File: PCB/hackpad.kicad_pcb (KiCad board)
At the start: 2 copper layers, 123.8 x 50 mm, 11 parts, among them SW1 SW_Push, SW2 SW_Push, SW3 SW_Push, SW4 SW_Push, SW5 SW_Push, SW7 SW_Push, U1 XIAO-RP2040-DIP

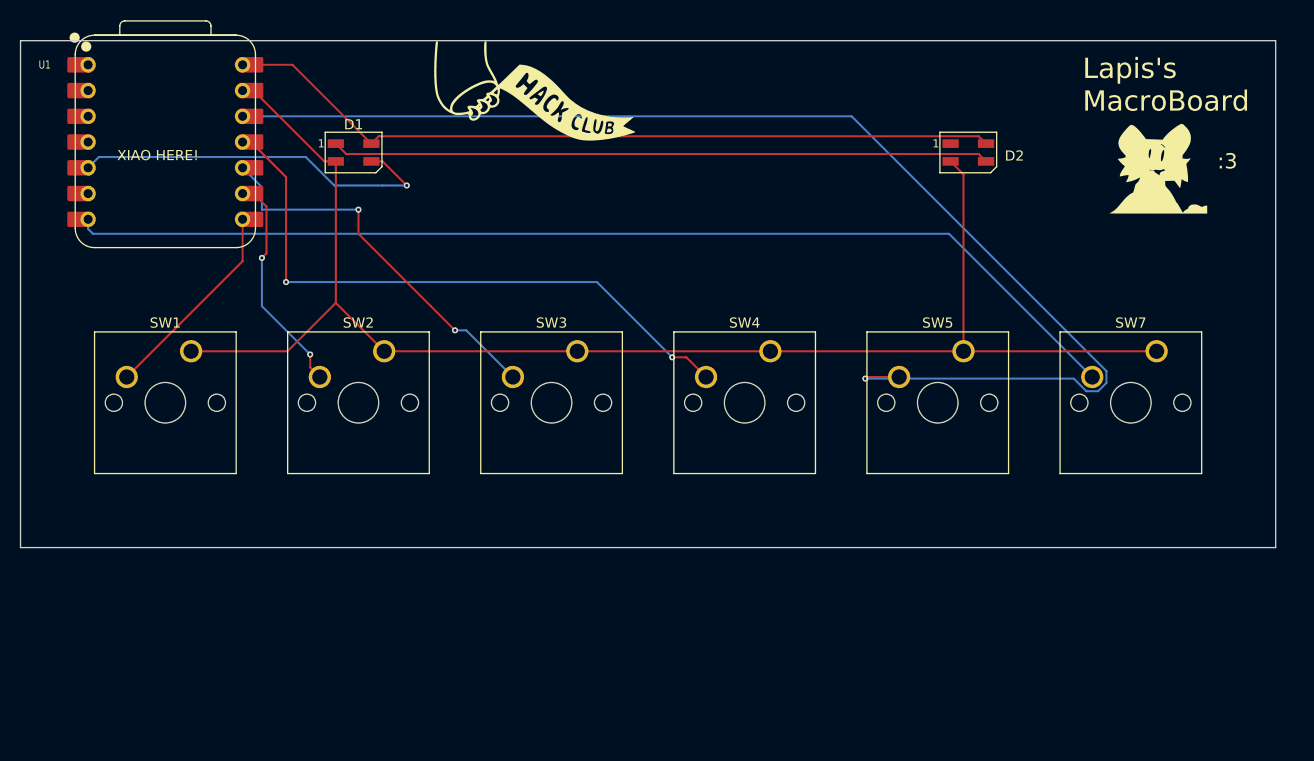
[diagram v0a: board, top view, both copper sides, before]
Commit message: push updated pcb and cad
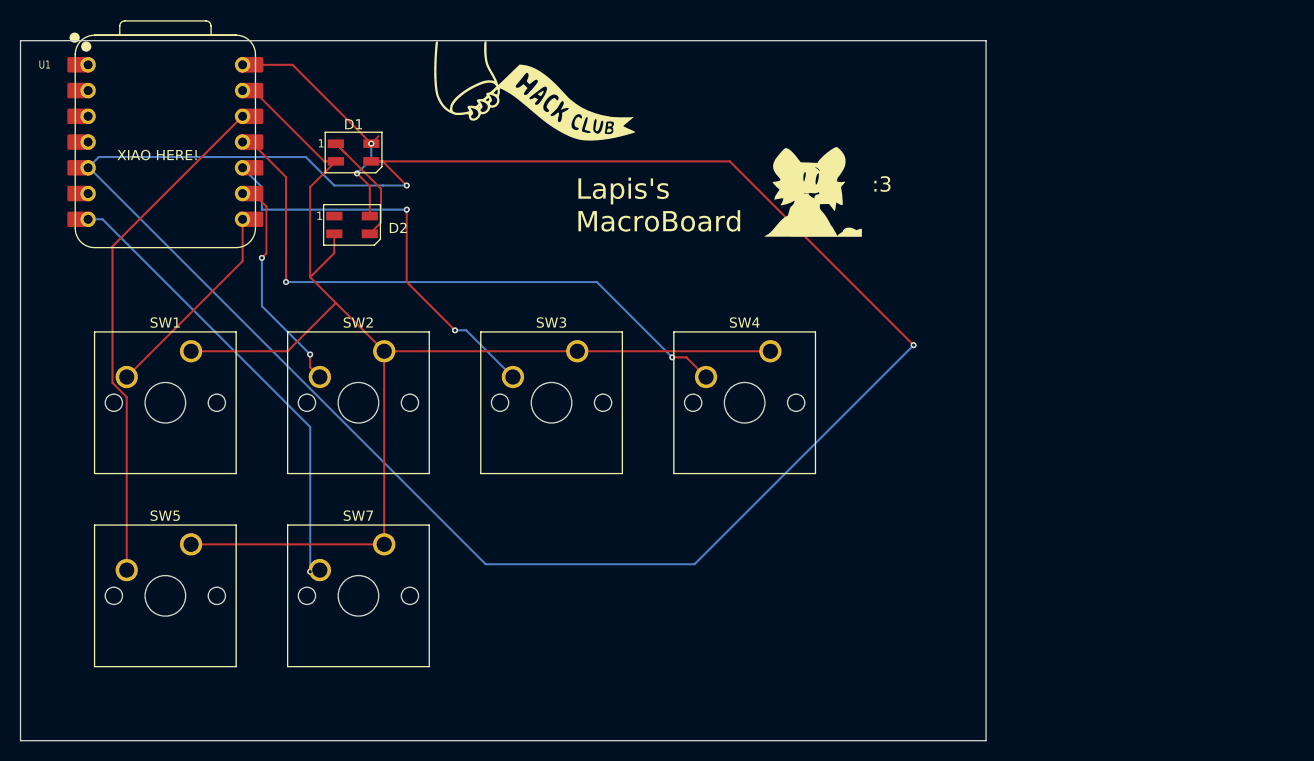
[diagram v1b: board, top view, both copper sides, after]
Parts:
- moved SW5 78.5 mm to (135.9, 114.0)
- moved SW7 78.5 mm to (154.9, 114.0)
- moved D2 61.2 mm to (151.8, 82.5)
- moved :3 34.1 mm to (196.9, 78.5)
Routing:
- net Net-(D1-DIN): track 37.5 -> 205.1 mm, vias 1 -> 2
- net Net-(U1-3V3): track 124.8 -> 50.7 mm, vias 1 -> 0
- net Net-(U1-GPIO0/TX): track 106.1 -> 45.7 mm, vias 0 -> 1
- net Net-(D1-DOUT): track 64.9 -> 12.6 mm
- net +5V: track 77.2 -> 25.2 mm, vias 0 -> 2
- net GND: track 144.5 -> 132.6 mm
- net Net-(U1-GPIO4/MISO): track 38.9 -> 41.7 mm
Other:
- board size 123.8 x 50 mm -> 95.2 x 69.1 mm
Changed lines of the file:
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@@
 	(footprint "LED_SMD:LED_SK6812MINI_PLCC4_3.5x3.5mm_P1.75mm"
 		(layer "F.Cu")
-		(at 212.5625 75.325)
+		(at 151.76875 82.46875)
 		(descr "3.5mm x 3.5mm PLCC4 Addressable RGB LED NeoPixel, https://cdn-shop.adafruit.com/product-files/2686/SK6812MINI_REV.01-1-2.pdf")
 		(tags "LED RGB NeoPixel Mini PLCC-4 3535")
@@
 	(footprint "Button_Switch_Keyboard:SW_Cherry_MX_1.00u_PCB"
 		(layer "F.Cu")
-		(at 231.14 94.9325)
+		(at 154.94 113.9825)
 		(descr "Cherry MX keyswitch, 1.00u, PCB mount, http://cherryamericas.com/wp-content/uploads/2014/12/mx_cat.pdf")
 		(tags "Cherry MX keyswitch 1.00u PCB")
@@
 	(footprint "LOGO"
 		(layer "F.Cu")
-		(at 230.98125 76.2)
+		(at 196.914142 78.488281)
 		(property "Reference" ":3"
 			(at 7.14375 0 0)
@@
 	(footprint "Button_Switch_Keyboard:SW_Cherry_MX_1.00u_PCB"
 		(layer "F.Cu")
-		(at 212.09 94.9325)
+		(at 135.89 113.9825)
 		(descr "Cherry MX keyswitch, 1.00u, PCB mount, http://cherryamericas.com/wp-content/uploads/2014/12/mx_cat.pdf")
 		(tags "Cherry MX keyswitch 1.00u PCB")
@@
 	(gr_rect
 		(start 119.0625 64.29375)
-		(end 242.8875 114.3)
+		(end 214.3125 133.35)
 		(stroke
 			(width 0.05)
@@
 	)
 	(gr_text "Lapis's \nMacroBoard"
-		(at 223.8375 71.4375 0)
+		(at 173.83125 83.34375 0)
 		(layer "F.SilkS")
 		(effects
@@
 	)
 	(segment
+		(start 135.89 113.9825)
+		(end 154.94 113.9825)
+		(width 0.2)
+		(layer "F.Cu")
+		(net 1)
+	)
+	(segment
 		(start 140.97 69.215)
 		(end 142.04763 69.215)
@@
 	)
 	(segment
-		(start 193.04 94.9325)
-		(end 212.09 94.9325)
+		(start 147.6375 87.63)
+		(end 150.17 90.1625)
 		(width 0.2)
 		(layer "F.Cu")
@@
 	)
 	(segment
+		(start 150.01875 83.34375)
+		(end 150.01875 85.24875)
+		(width 0.2)
+		(layer "F.Cu")
+		(net 1)
+	)
+	(segment
 		(start 145.4 94.9325)
 		(end 150.17 90.1625)
@@
 	)
 	(segment
-		(start 135.89 94.9325)
-		(end 145.4 94.9325)
+		(start 154.94 113.9825)
+		(end 154.94 94.9325)
 		(width 0.2)
 		(layer "F.Cu")
@@
 	)
 	(segment
-		(start 212.09 77.4775)
-		(end 210.8125 76.2)
+		(start 150.01875 85.24875)
+		(end 147.6375 87.63)
 		(width 0.2)
 		(layer "F.Cu")
@@
 	)
 	(segment
-		(start 150.17 76.2)
-		(end 150.17 90.1625)
+		(start 135.89 94.9325)
+		(end 145.4 94.9325)
 		(width 0.2)
 		(layer "F.Cu")
@@
 	)
 	(segment
-		(start 212.09 94.9325)
-		(end 212.09 77.4775)
+		(start 150.17 76.2)
+		(end 147.6375 78.7325)
 		(width 0.2)
 		(layer "F.Cu")
@@
 	)
 	(segment
-		(start 212.09 94.9325)
-		(end 231.14 94.9325)
+		(start 147.6375 78.7325)
+		(end 147.6375 87.63)
 		(width 0.2)
 		(layer "F.Cu")
@@
 	)
 	(segment
-		(start 151.194 75.474)
-		(end 213.5865 75.474)
+		(start 154.61975 82.24275)
+		(end 154.61975 78.89975)
 		(width 0.2)
 		(layer "F.Cu")
@@
 	)
 	(segment
-		(start 213.5865 75.474)
-		(end 214.3125 76.2)
+		(start 153.51875 83.34375)
+		(end 154.61975 82.24275)
 		(width 0.2)
 		(layer "F.Cu")
@@
 	)
 	(segment
+		(start 154.61975 78.89975)
+		(end 150.17 74.45)
+		(width 0.2)
+		(layer "F.Cu")
+		(net 2)
+	)
+	(segment
 		(start 140.97 66.675)
 		(end 145.895 66.675)
@@
 	)
 	(segment
-		(start 213.5865 73.724)
-		(end 214.3125 74.45)
+		(start 153.51875 78.64728)
+		(end 152.259285 77.387815)
+		(width 0.2)
+		(layer "F.Cu")
+		(net 3)
+	)
+	(segment
+		(start 153.51875 81.59375)
+		(end 153.51875 78.64728)
 		(width 0.2)
 		(layer "F.Cu")
@@
 		(net 3)
 	)
+	(via
+		(at 153.67 74.45)
+		(size 0.6)
+		(drill 0.3)
+		(layers "F.Cu" "B.Cu")
+		(net 3)
+	)
+	(via
+		(at 152.259285 77.387815)
+		(size 0.6)
+		(drill 0.3)
+		(layers "F.Cu" "B.Cu")
+		(net 3)
+	)
 	(segment
-		(start 154.396 73.724)
-		(end 213.5865 73.724)
+		(start 152.259285 77.387815)
+		(end 153.67 75.9771)
 		(width 0.2)
-		(layer "F.Cu")
+		(layer "B.Cu")
 		(net 3)
 	)
 	(segment
+		(start 153.67 75.9771)
+		(end 153.67 74.45)
+		(width 0.2)
+		(layer "B.Cu")
+		(net 3)
+	)
+	(segment
+		(start 189.03625 76.2)
+		(end 207.16875 94.3325)
+		(width 0.2)
+		(layer "F.Cu")
+		(net 4)
+	)
+	(segment
+		(start 153.67 76.2)
+		(end 189.03625 76.2)
+		(width 0.2)
+		(layer "F.Cu")
+		(net 4)
+	)
+	(segment
 		(start 157.1625 78.58125)
 		(end 154.78125 76.2)
@@
 	)
 	(via
+		(at 207.16875 94.3325)
+		(size 0.6)
+		(drill 0.3)
+		(layers "F.Cu" "B.Cu")
+		(net 4)
+	)
+	(via
 		(at 157.1625 78.58125)
 		(size 0.6)
@@
 	)
 	(segment
+		(start 164.948156 115.942186)
+		(end 125.84097 76.835)
+		(width 0.2)
+		(layer "B.Cu")
+		(net 4)
+	)
+	(segment
+		(start 125.84097 76.835)
+		(end 125.73 76.835)
+		(width 0.2)
+		(layer "B.Cu")
+		(net 4)
+	)
+	(segment
 		(start 150.01875 78.58125)
 		(end 154.78125 78.58125)
@@
 	)
 	(segment
+		(start 207.16875 94.3325)
+		(end 185.559064 115.942186)
+		(width 0.2)
+		(layer "B.Cu")
+		(net 4)
+	)
+	(segment
+		(start 185.559064 115.942186)
+		(end 164.948156 115.942186)
+		(width 0.2)
+		(layer "B.Cu")
+		(net 4)
+	)
+	(segment
 		(start 129.54 97.4725)
 		(end 140.97 86.0425)
@@
 	)
 	(segment
-		(start 159.54375 90.4875)
-		(end 161.925 92.86875)
-		(width 0.2)
-		(layer "F.Cu")
-		(net 8)
-	)
-	(segment
 		(start 167.48125 97.63125)
 		(end 167.64 97.4725)
@@
 	)
 	(segment
-		(start 152.4 83.34375)
-		(end 152.4 80.9625)
+		(start 157.1625 88.10625)
+		(end 161.925 92.86875)
 		(width 0.2)
 		(layer "F.Cu")
@@
 	)
 	(segment
-		(start 159.54375 90.4875)
-		(end 152.4 83.34375)
+		(start 157.1625 80.9625)
+		(end 157.1625 88.10625)
 		(width 0.2)
 		(layer "F.Cu")
@@
 	)
 	(via
-		(at 152.4 80.9625)
+		(at 157.1625 80.9625)
 		(size 0.6)
 		(drill 0.3)
@@
 	)
 	(segment
-		(start 152.4 80.9625)
-		(end 142.875 80.9625)
+		(start 142.875 78.74)
+		(end 140.97 76.835)
 		(width 0.2)
 		(layer "B.Cu")
@@
 	)
 	(segment
-		(start 142.875 80.9625)
-		(end 142.875 78.74)
+		(start 157.1625 80.9625)
+		(end 142.875 80.9625)
 		(width 0.2)
 		(layer "B.Cu")
@@
 	)
 	(segment
-		(start 142.875 78.74)
-		(end 140.97 76.835)
+		(start 161.925 92.86875)
+		(end 163.03625 92.86875)
 		(width 0.2)
 		(layer "B.Cu")
@@
 	)
 	(segment
-		(start 161.925 92.86875)
-		(end 163.03625 92.86875)
+		(start 142.875 80.9625)
+		(end 142.875 78.74)
 		(width 0.2)
 		(layer "B.Cu")
@@
 	)
 	(segment
-		(start 202.565 97.4725)
-		(end 202.40625 97.63125)
+		(start 129.54 99.453814)
+		(end 128.139 98.052814)
 		(width 0.2)
 		(layer "F.Cu")
@@
 	)
 	(segment
-		(start 205.74 97.4725)
-		(end 202.565 97.4725)
+		(start 129.54 116.5225)
+		(end 129.54 99.453814)
 		(width 0.2)
 		(layer "F.Cu")
 		(net 10)
 	)
-	(via
-		(at 202.40625 97.63125)
-		(size 0.6)
-		(drill 0.3)
-		(layers "F.Cu" "B.Cu")
-		(net 10)
-	)
-	(segment
-		(start 226.191 98.052814)
-		(end 226.191 96.892186)
-		(width 0.2)
-		(layer "B.Cu")
-		(net 10)
-	)
 	(segment
-		(start 224.209686 98.8735)
-		(end 225.370314 98.8735)
-		(width 0.2)
-		(layer "B.Cu")
-		(net 10)
-	)
-	(segment
-		(start 202.40625 97.63125)
-		(end 222.967436 97.63125)
-		(width 0.2)
-		(layer "B.Cu")
-		(net 10)
-	)
-	(segment
-		(start 226.191 96.892186)
-		(end 201.053814 71.755)
+		(start 128.139 84.586)
+		(end 140.97 71.755)
 		(width 0.2)
-		(layer "B.Cu")
+		(layer "F.Cu")
 		(net 10)
 	)
 	(segment
-		(start 225.370314 98.8735)
-		(end 226.191 98.052814)
+		(start 128.139 98.052814)
+		(end 128.139 84.586)
 		(width 0.2)
-		(layer "B.Cu")
+		(layer "F.Cu")
 		(net 10)
 	)
 	(segment
-		(start 201.053814 71.755)
-		(end 140.97 71.755)
+		(start 147.79625 116.5225)
+		(end 147.6375 116.68125)
 		(width 0.2)
-		(layer "B.Cu")
-		(net 10)
+		(layer "F.Cu")
+		(net 14)
 	)
 	(segment
-		(start 222.967436 97.63125)
-		(end 224.209686 98.8735)
+		(start 148.59 116.5225)
+		(end 147.79625 116.5225)
 		(width 0.2)
-		(layer "B.Cu")
-		(net 10)
+		(layer "F.Cu")
+		(net 14)
 	)
-	(segment
-		(start 126.20625 83.34375)
-		(end 125.73 82.8675)
-		(width 0.2)
-		(layer "B.Cu")
+	(via
+		(at 147.6375 116.68125)
+		(size 0.6)
+		(drill 0.3)
+		(layers "F.Cu" "B.Cu")
 		(net 14)
 	)
 	(segment
-		(start 125.73 82.8675)
+		(start 127.15875 81.915)
 		(end 125.73 81.915)
 		(width 0.2)
@@
 	)
 	(segment
-		(start 210.66125 83.34375)
-		(end 126.20625 83.34375)
+		(start 147.6375 116.68125)
+		(end 147.6375 102.39375)
 		(width 0.2)
 		(layer "B.Cu")
@@
 	)
 	(segment
-		(start 224.79 97.4725)
-		(end 210.66125 83.34375)
+		(start 147.6375 102.39375)
+		(end 127.15875 81.915)
 		(width 0.2)
 		(layer "B.Cu")

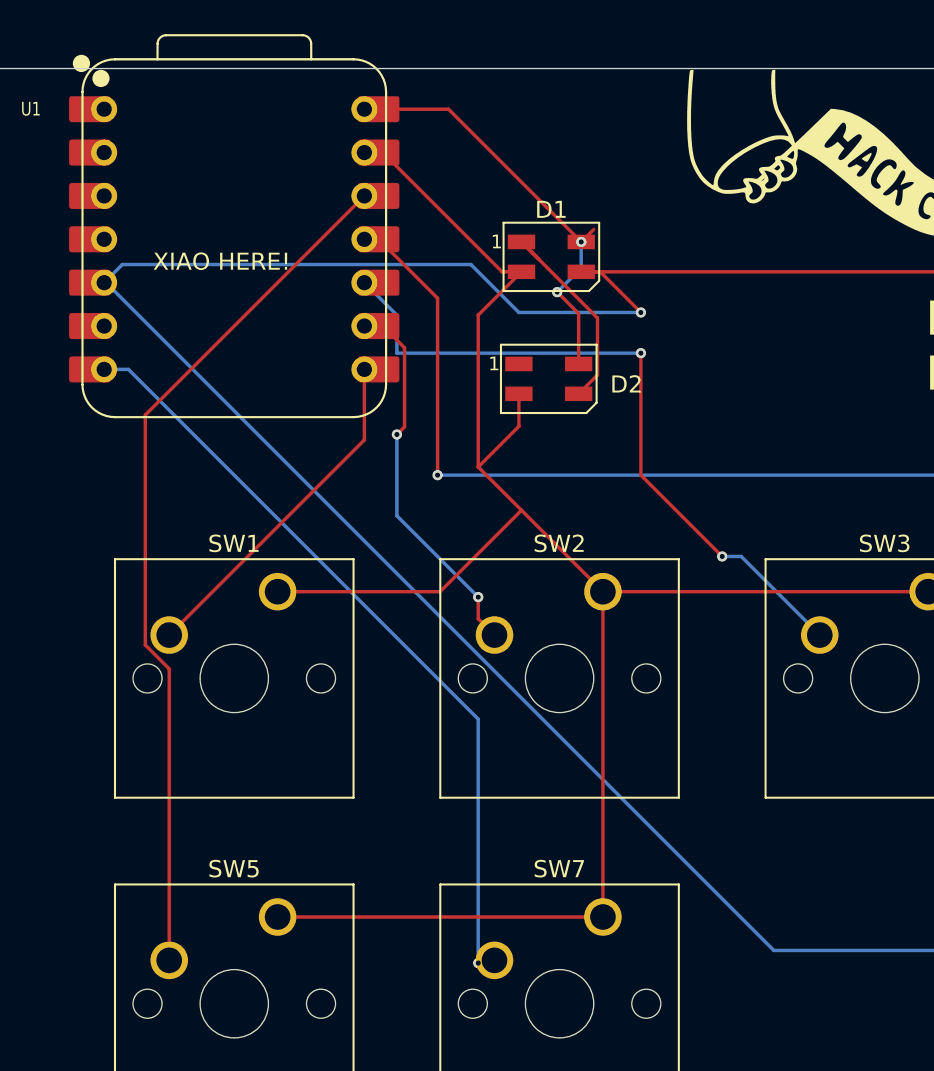
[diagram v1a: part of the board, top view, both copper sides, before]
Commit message: update pcb + schematic to not short the entire board (...oops)
readme update soon
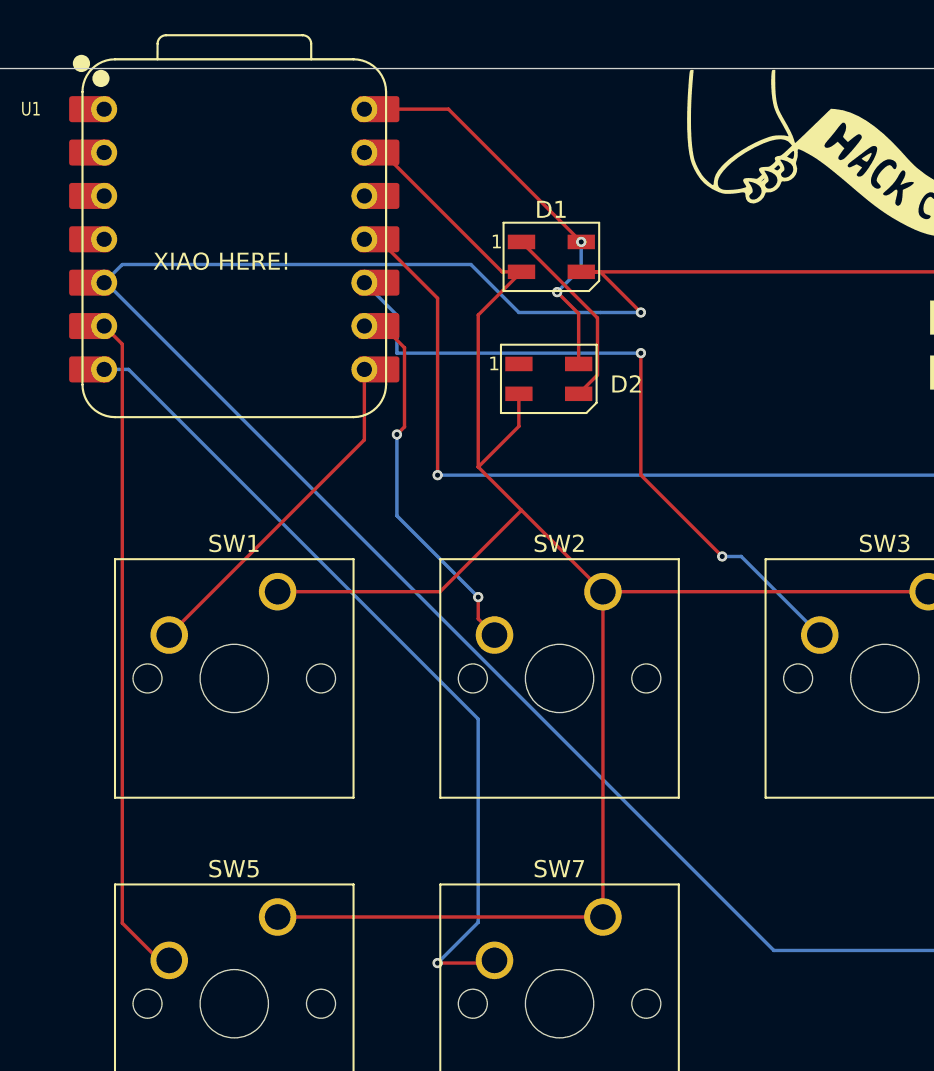
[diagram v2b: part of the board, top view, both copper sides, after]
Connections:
- SW5 pad 2: Net-(U1-3V3) -> Net-(U1-GPIO7/SCL)
- U1 pad 12: Net-(U1-3V3) -> unconnected-(U1-3V3-Pad12)
- U1 pad 6: unconnected-(U1-GPIO7/SCL-Pad6) -> Net-(U1-GPIO7/SCL)
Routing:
- net Net-(U1-3V3): track 50.7 -> 0.00 mm
- net Net-(U1-GPIO7/SCL): track 0.00 -> 38.9 mm
- net Net-(U1-GPIO0/TX): track 45.7 -> 49.1 mm
- net Net-(D1-DOUT): track 12.6 -> 11.2 mm
- net +5V: track 25.2 -> 24.2 mm
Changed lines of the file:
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@@
 	(net 8 "Net-(U1-GPIO4{slash}MISO)")
 	(net 9 "Net-(U1-GPIO3{slash}MOSI)")
-	(net 10 "Net-(U1-3V3)")
-	(net 11 "unconnected-(U1-GPIO7{slash}SCL-Pad6)")
+	(net 10 "Net-(U1-GPIO7{slash}SCL)")
+	(net 11 "unconnected-(U1-3V3-Pad12)")
 	(net 12 "unconnected-(U1-GPIO26{slash}ADC0{slash}A0-Pad1)")
 	(net 13 "unconnected-(U1-GPIO29{slash}ADC3{slash}A3-Pad4)")
@@
 		(at 169.754101 70.000013)
 		(property "Reference" "_"
-			(at -2.400278 -2.438086 0)
+			(at -2.400278 1.437487 0)
 			(layer "F.SilkS")
+			(hide yes)
 			(effects
 				(font
@@
 			(layers "F.Cu" "F.Mask")
 			(roundrect_rratio 0.1)
-			(net 11 "unconnected-(U1-GPIO7{slash}SCL-Pad6)")
+			(net 10 "Net-(U1-GPIO7{slash}SCL)")
 			(pinfunction "GPIO7/SCL")
 			(pintype "passive")
@@
 			(layers "*.Cu" "*.Mask")
 			(remove_unused_layers no)
-			(net 11 "unconnected-(U1-GPIO7{slash}SCL-Pad6)")
+			(net 10 "Net-(U1-GPIO7{slash}SCL)")
 			(pinfunction "GPIO7/SCL")
 			(pintype "passive")
@@
 			(layers "*.Cu" "*.Mask")
 			(remove_unused_layers no)
-			(net 10 "Net-(U1-3V3)")
+			(net 11 "unconnected-(U1-3V3-Pad12)")
 			(pinfunction "3V3")
 			(pintype "passive")
@@
 			(layers "F.Cu" "F.Mask")
 			(roundrect_rratio 0.1)
-			(net 10 "Net-(U1-3V3)")
+			(net 11 "unconnected-(U1-3V3-Pad12)")
 			(pinfunction "3V3")
 			(pintype "passive")
@@
 			(layers "*.Cu" "*.Mask")
 			(remove_unused_layers no)
-			(net 10 "Net-(U1-3V3)")
+			(net 10 "Net-(U1-GPIO7{slash}SCL)")
 			(pinfunction "2")
 			(pintype "passive")
@@
 	)
 	(segment
-		(start 150.17 74.45)
-		(end 151.194 75.474)
-		(width 0.2)
-		(layer "F.Cu")
-		(net 2)
-	)
-	(segment
 		(start 154.61975 78.89975)
 		(end 150.17 74.45)
@@
 		(net 3)
 	)
-	(segment
-		(start 153.67 74.45)
-		(end 154.396 73.724)
-		(width 0.2)
-		(layer "F.Cu")
-		(net 3)
-	)
 	(via
 		(at 153.67 74.45)
@@
 	)
 	(segment
-		(start 129.54 99.453814)
-		(end 128.139 98.052814)
+		(start 126.793 114.3426)
+		(end 129.25645 116.80605)
 		(width 0.2)
 		(layer "F.Cu")
@@
 	)
 	(segment
-		(start 129.54 116.5225)
-		(end 129.54 99.453814)
+		(start 126.793 80.438)
+		(end 126.793 114.3426)
 		(width 0.2)
 		(layer "F.Cu")
@@
 	)
 	(segment
-		(start 128.139 84.586)
-		(end 140.97 71.755)
+		(start 125.73 79.375)
+		(end 126.793 80.438)
 		(width 0.2)
 		(layer "F.Cu")
@@
 	)
 	(segment
-		(start 128.139 98.052814)
-		(end 128.139 84.586)
+		(start 147.6375 116.68125)
+		(end 147.79625 116.5225)
 		(width 0.2)
 		(layer "F.Cu")
-		(net 10)
+		(net 14)
 	)
 	(segment
-		(start 147.79625 116.5225)
+		(start 145.25625 116.68125)
 		(end 147.6375 116.68125)
 		(width 0.2)
@@
 	)
 	(segment
-		(start 148.59 116.5225)
-		(end 147.79625 116.5225)
+		(start 147.79625 116.5225)
+		(end 148.59 116.5225)
 		(width 0.2)
 		(layer "F.Cu")
@@
 	)
 	(via
-		(at 147.6375 116.68125)
+		(at 145.25625 116.68125)
 		(size 0.6)
 		(drill 0.3)
@@
 	)
 	(segment
-		(start 127.15875 81.915)
-		(end 125.73 81.915)
+		(start 147.6375 114.3)
+		(end 147.6375 102.39375)
 		(width 0.2)
 		(layer "B.Cu")
@@
 	)
 	(segment
-		(start 147.6375 116.68125)
-		(end 147.6375 102.39375)
+		(start 145.25625 116.68125)
+		(end 147.6375 114.3)
 		(width 0.2)
 		(layer "B.Cu")
@@
 		(width 0.2)
 		(layer "B.Cu")
+		(net 14)
+	)
+	(segment
+		(start 127.15875 81.915)
+		(end 125.73 81.915)
+		(width 0.2)
+		(layer "B.Cu")
